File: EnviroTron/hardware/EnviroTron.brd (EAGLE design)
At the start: 27.3 x 36.8 mm, 38 parts

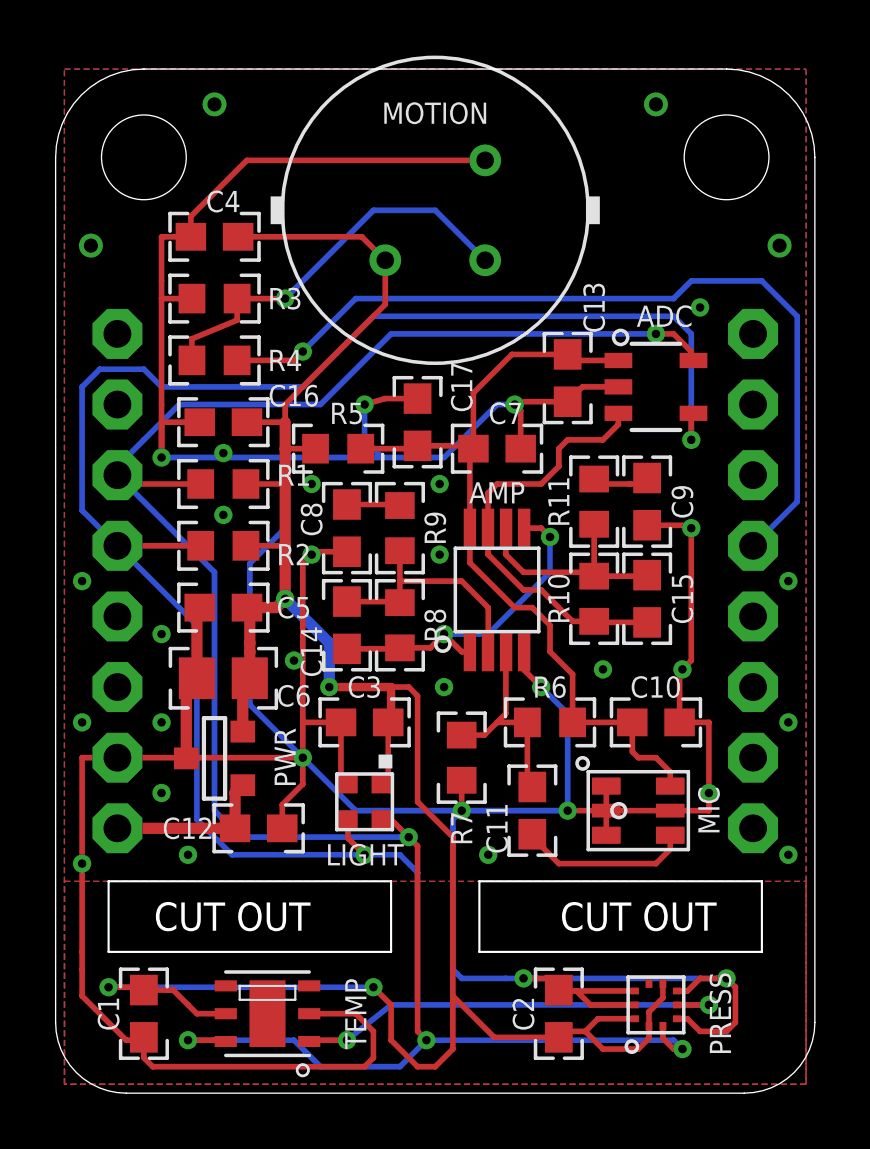
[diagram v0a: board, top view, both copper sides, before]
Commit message: Added PI filter to create analog voltage rail. Increased mic amp gain. Replaced mic with lower noise device.
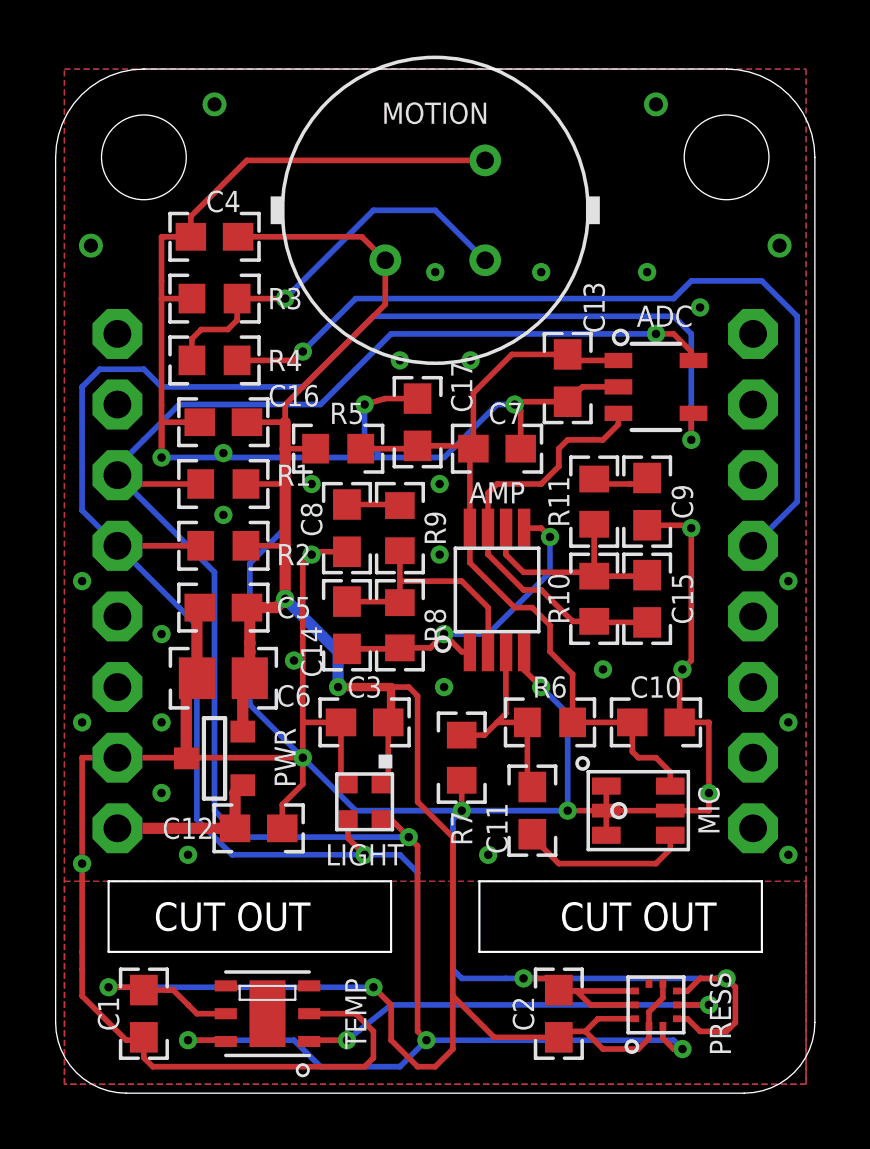
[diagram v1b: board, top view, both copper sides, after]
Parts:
- AMP: value MCP6002 -> OPAMP-OPA2376-MSOP8
- C11: value 100n -> 10n
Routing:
- net GND: vias 37 -> 42
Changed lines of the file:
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@@
 <attribute name="PN-DK" value="1649-1005-1-ND" x="7.62" y="2.8575" size="1.778" layer="27" rot="R90" display="off"/>
 </element>
-<element name="COMMS" library="EnviroTron" package="WEMOS-D1-MINI" value="WEMOS-D1-MINI" x="13.6525" y="18.415" smashed="yes" rot="MR0"/>
+<element name="COMMS" library="EnviroTron" package="WEMOS-D1-MINI" value="WEMOS-D1-MINI" x="13.6525" y="18.415" smashed="yes" rot="MR0">
+<attribute name="SPICEPREFIX" value="X" x="13.6525" y="18.415" size="1.778" layer="28" rot="MR0" display="off"/>
+</element>
 <element name="PRESS" library="EnviroTron" package="HLGA-10L" value="LPS22HB" x="21.59" y="3.175" smashed="yes" rot="R90">
 <attribute name="MFG" value="STMicroelectronics" x="21.59" y="3.175" size="1.778" layer="27" rot="R90" display="off"/>
@@
 <attribute name="VALUE" x="19.3675" y="21.2725" size="1.016" layer="27" rot="R90" align="center"/>
 </element>
-<element name="C11" library="EnviroTron" package="C0603" value="100n" x="17.145" y="10.16" smashed="yes" rot="R90">
+<element name="C11" library="EnviroTron" package="C0603" value="10n" x="17.145" y="10.16" smashed="yes" rot="R90">
 <attribute name="NAME" x="15.875" y="9.525" size="0.762" layer="25" rot="R90" align="center"/>
 <attribute name="VALUE" x="17.145" y="10.16" size="1.016" layer="27" rot="R90" align="center"/>
@@
 <attribute name="VALUE" x="13.0175" y="24.13" size="1.016" layer="27" rot="R90" align="center"/>
 </element>
-<element name="AMP" library="EnviroTron" package="MSOP-8" value="MCP6002" x="15.875" y="18.0975" smashed="yes">
-<attribute name="MFG" value="Microchip Technology" x="15.875" y="18.0975" size="1.778" layer="27" display="off"/>
-<attribute name="MPN" value="MCP6002T-I/MS" x="15.875" y="18.0975" size="1.778" layer="27" display="off"/>
+<element name="AMP" library="EnviroTron" package="MSOP-8" value="OPAMP-OPA2376-MSOP8" x="15.875" y="18.0975" smashed="yes">
+<attribute name="MFG" value="Texas Instruments" x="15.875" y="18.0975" size="1.778" layer="27" display="off"/>
+<attribute name="MPN" value="OPA2376AIDGKR" x="15.875" y="18.0975" size="1.778" layer="27" display="off"/>
 <attribute name="NAME" x="15.875" y="21.59" size="0.762" layer="25" align="center"/>
-<attribute name="PN-DK" value="MCP6002T-I/MSCT-ND" x="15.875" y="18.0975" size="1.778" layer="27" display="off"/>
+<attribute name="PN-DK" value="296-22630-1-ND" x="15.875" y="18.0975" size="1.778" layer="27" display="off"/>
+<attribute name="SPICEPREFIX" value="J" x="15.875" y="18.0975" size="1.778" layer="27" display="off"/>
 <attribute name="VALUE" x="15.875" y="18.0975" size="1.016" layer="27" align="center"/>
 </element>
@@
 <contactref element="C6" pad="1"/>
 <contactref element="C5" pad="1"/>
-<wire x1="8.255" y1="17.78" x2="9.8425" y2="16.1925" width="0.4064" layer="16"/>
-<wire x1="9.8425" y1="16.1925" x2="9.8425" y2="14.605" width="0.4064" layer="16"/>
-<wire x1="9.8425" y1="14.605" x2="12.065" y2="14.605" width="0.3048" layer="1"/>
+<wire x1="8.255" y1="17.78" x2="10.16" y2="15.875" width="0.4064" layer="16"/>
+<wire x1="10.16" y1="15.875" x2="10.16" y2="14.605" width="0.4064" layer="16"/>
+<wire x1="10.16" y1="14.605" x2="12.065" y2="14.605" width="0.3048" layer="1"/>
 <contactref element="PWR" pad="2"/>
 <wire x1="6.985" y1="16.1925" x2="6.985" y2="17.36" width="0.4064" layer="1"/>
@@
 <wire x1="13.0175" y1="14.2875" x2="12.7" y2="14.605" width="0.2032" layer="1"/>
 <wire x1="12.7" y1="14.605" x2="12.065" y2="14.605" width="0.2032" layer="1"/>
-<via x="9.8425" y="14.605" extent="1-16" drill="0.3048"/>
+<via x="10.16" y="14.605" extent="1-16" drill="0.3048"/>
 <wire x1="6.731" y1="13.0048" x2="6.731" y2="14.671" width="0.4064" layer="1"/>
 <wire x1="6.731" y1="14.671" x2="6.9825" y2="14.9225" width="0.4064" layer="1"/>
@@
 <via x="19.685" y="15.24" extent="1-16" drill="0.3048"/>
 <via x="23.495" y="10.795" extent="1-16" drill="0.3048"/>
+<via x="12.3825" y="26.3525" extent="1-16" drill="0.3048"/>
+<via x="14.9225" y="26.3525" extent="1-16" drill="0.3048"/>
+<via x="13.6525" y="29.5275" extent="1-16" drill="0.3048"/>
+<via x="17.4625" y="29.5275" extent="1-16" drill="0.3048"/>
+<via x="21.2725" y="29.5275" extent="1-16" drill="0.3048"/>
 </signal>
 <signal name="PIROUT">
@@
 <wire x1="4.9022" y1="27.1272" x2="4.9022" y2="26.3525" width="0.2032" layer="1"/>
 <wire x1="6.5278" y1="28.575" x2="6.5278" y2="27.8003" width="0.2032" layer="1"/>
-<wire x1="6.5278" y1="27.8003" x2="4.9022" y2="27.1272" width="0.2032" layer="1"/>
+<wire x1="6.5278" y1="27.8003" x2="6.19125" y2="27.46375" width="0.2032" layer="1"/>
+<wire x1="6.19125" y1="27.46375" x2="5.23875" y2="27.46375" width="0.2032" layer="1"/>
+<wire x1="5.23875" y1="27.46375" x2="4.9022" y2="27.1272" width="0.2032" layer="1"/>
 <wire x1="6.5278" y1="28.575" x2="8.255" y2="28.575" width="0.2032" layer="1"/>
 <via x="8.255" y="28.575" extent="1-16" drill="0.3048"/>
